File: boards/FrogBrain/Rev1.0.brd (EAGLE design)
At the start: 51 x 51 mm, 14 parts, among them U1 PIC16F1778, U2 AT25SF321, U3 ADP7104

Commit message: Final rev 1.0 brain and initial tadpole breadboard.
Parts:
- moved JP1 1.15 mm to (30.3, 4.94)
- renumbered U$4 to SW
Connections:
- net GND: now also JP4.1, JP4.2, JP4.3, JP5.4, JP5.8
- net SCK: now also JP5.7; no longer JP4.3
- net SI: now also JP5.5; no longer JP4.5
- net SO: now also JP5.6; no longer JP4.4
- net UARTRX: now also JP4.4; no longer JP4.1
- net UARTTX: now also JP4.5; no longer JP4.2
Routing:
- net SCK: track 76.2 -> 50.2 mm
- net UARTTX: track 68.2 -> 49.3 mm
- net UARTRX: track 85.1 -> 66.9 mm
- net SO: track 72.8 -> 59.2 mm
- net ~MCLR: track 70.9 -> 79.2 mm
- net SI: track 59.2 -> 52.0 mm
- net RC6: track 30.6 -> 35.8 mm
- net RC5: track 43.2 -> 45.8 mm
- net VIN: track 49.9 -> 48.0 mm
- net ICSPCLK: track 76.1 -> 75.1 mm
- net ICSPDAT: track 96.2 -> 97.0 mm
- net N$12: track 47.9 -> 47.2 mm
- net FLASHSEL: track 49.4 -> 50.1 mm, vias 0 -> 1
- net N$11: track 18.2 -> 17.6 mm

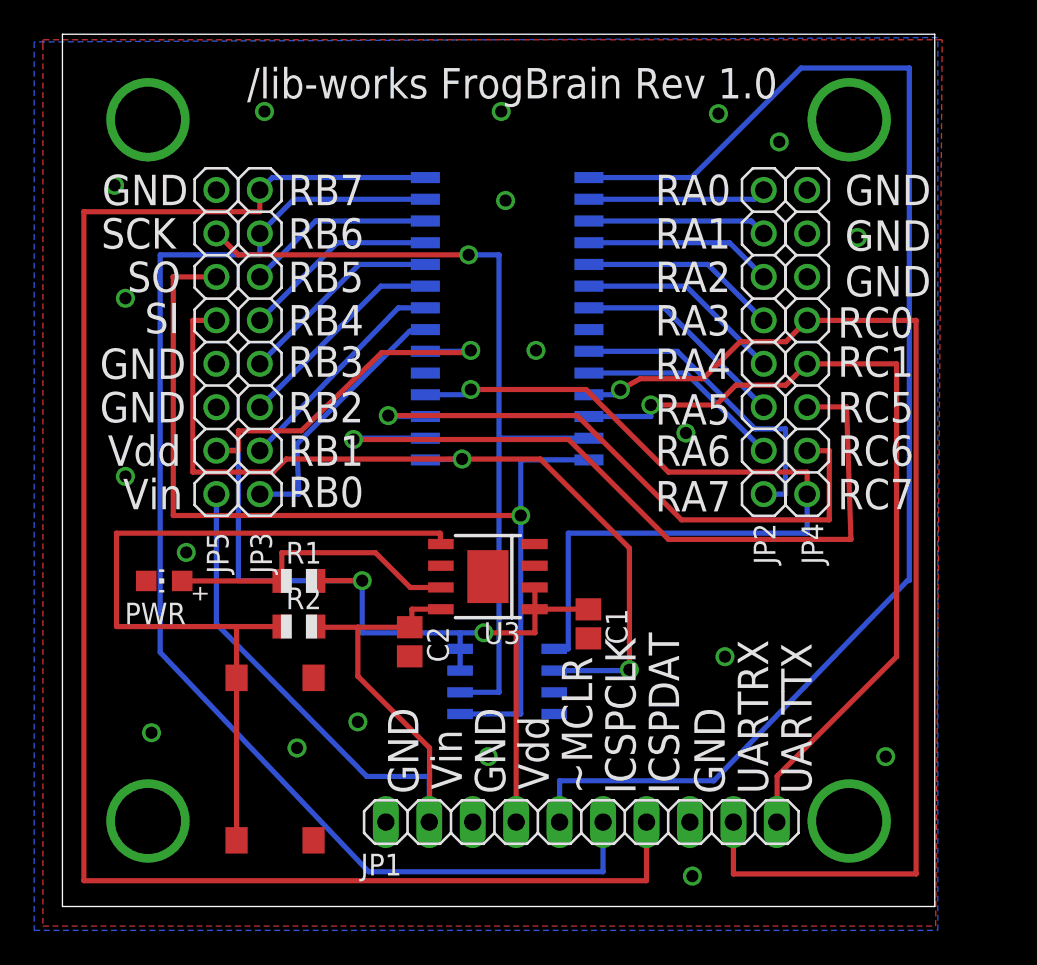
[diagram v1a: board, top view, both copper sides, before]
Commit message: Kermit PIC protocol and small frogbrain board mods.
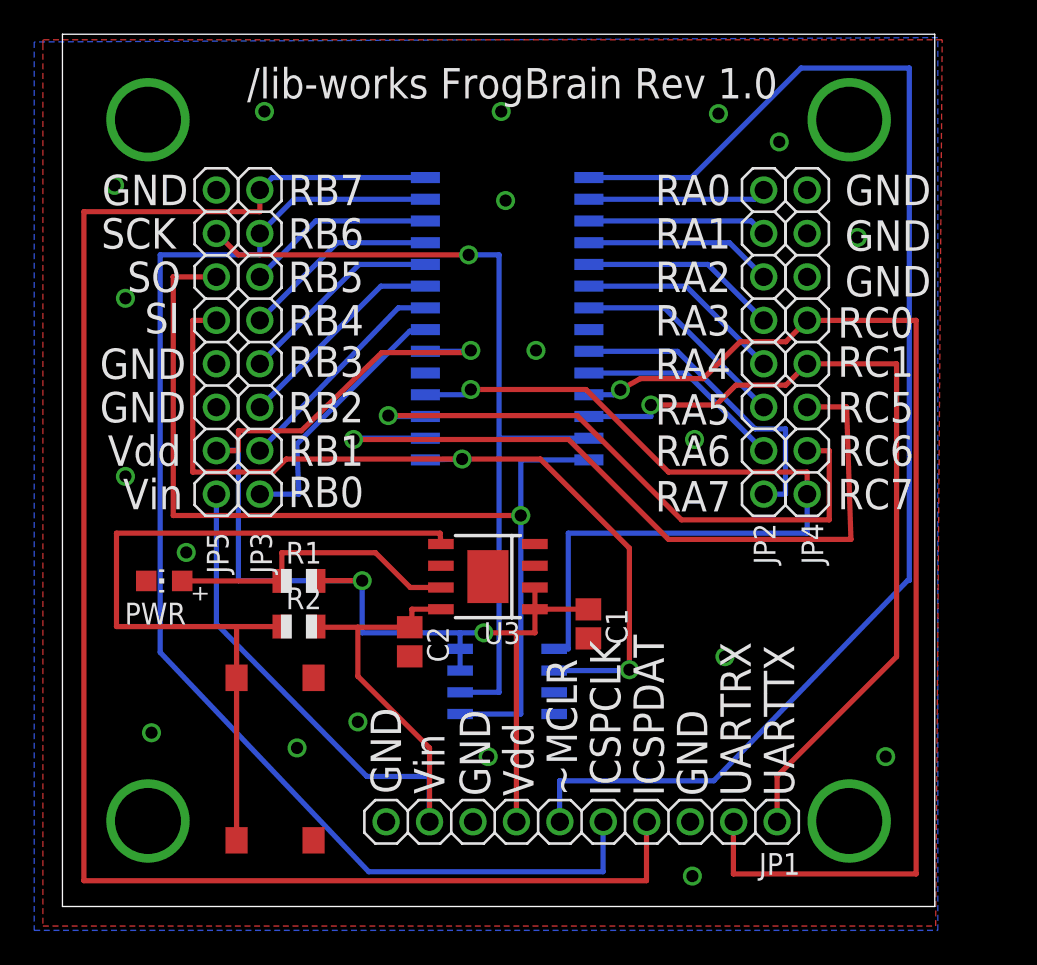
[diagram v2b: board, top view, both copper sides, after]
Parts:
- JP1: value (none) -> HEADER-1X10; device pinhead:1X10 -> lib-works:1X10
- R1: value 100 -> 160
- moved JP1 2.56 mm to (32.9, 4.95), turned to 180 degrees
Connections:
- net GND: now also JP1.10; no longer JP1.1
- net ICSPCLK: now also JP1.5; no longer JP1.6
- net ICSPDAT: now also JP1.4; no longer JP1.7
- net UARTRX: now also JP1.2; no longer JP1.9
- net UARTTX: now also JP1.1; no longer JP1.10
- net VDD: now also JP1.7; no longer JP1.4
- net VIN: now also JP1.9; no longer JP1.2
- net ~MCLR: now also JP1.6; no longer JP1.5
